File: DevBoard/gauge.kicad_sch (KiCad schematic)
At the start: 44 parts, among them J101 Pack (welded 4S) - use instea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, J102 Cell NTC 10k 103AT, J103 EV2400 SMBus, Q101 AGM404AP1, Q102 AGM404AP1, U101 BQ40Z50RSMR-R2

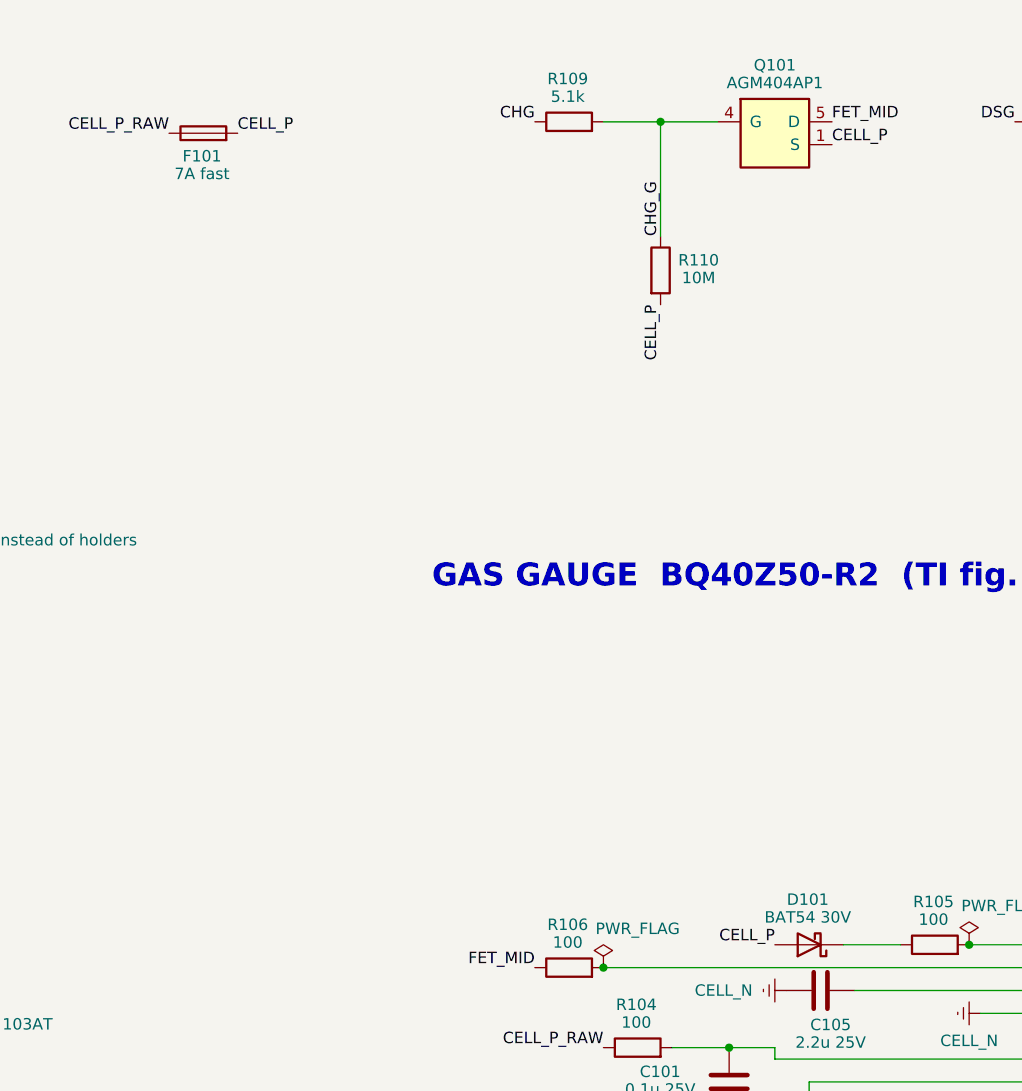
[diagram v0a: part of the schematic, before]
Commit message: Dev board: choose fuse, gauge diode and TPS25751 capacitor values
- F101: 1206FA-8A (C21261118), 1206, 32 V, 300 A interrupt; D101: BAT54WS (C7502694)
- TPS25751 caps per datasheet table 6.4 (after derating): LDO_3V3 and LDO_1V5
  to 10 uF, VBUS to 4.7 uF 50 V 0805, PP5V bulk to a 220 uF polymer
- README: PPHV bulk vs cSnkBulkPd and INA190 stock as open items

Co-Authored-By: Claude Opus 5.5 <noreply@anthropic.com>
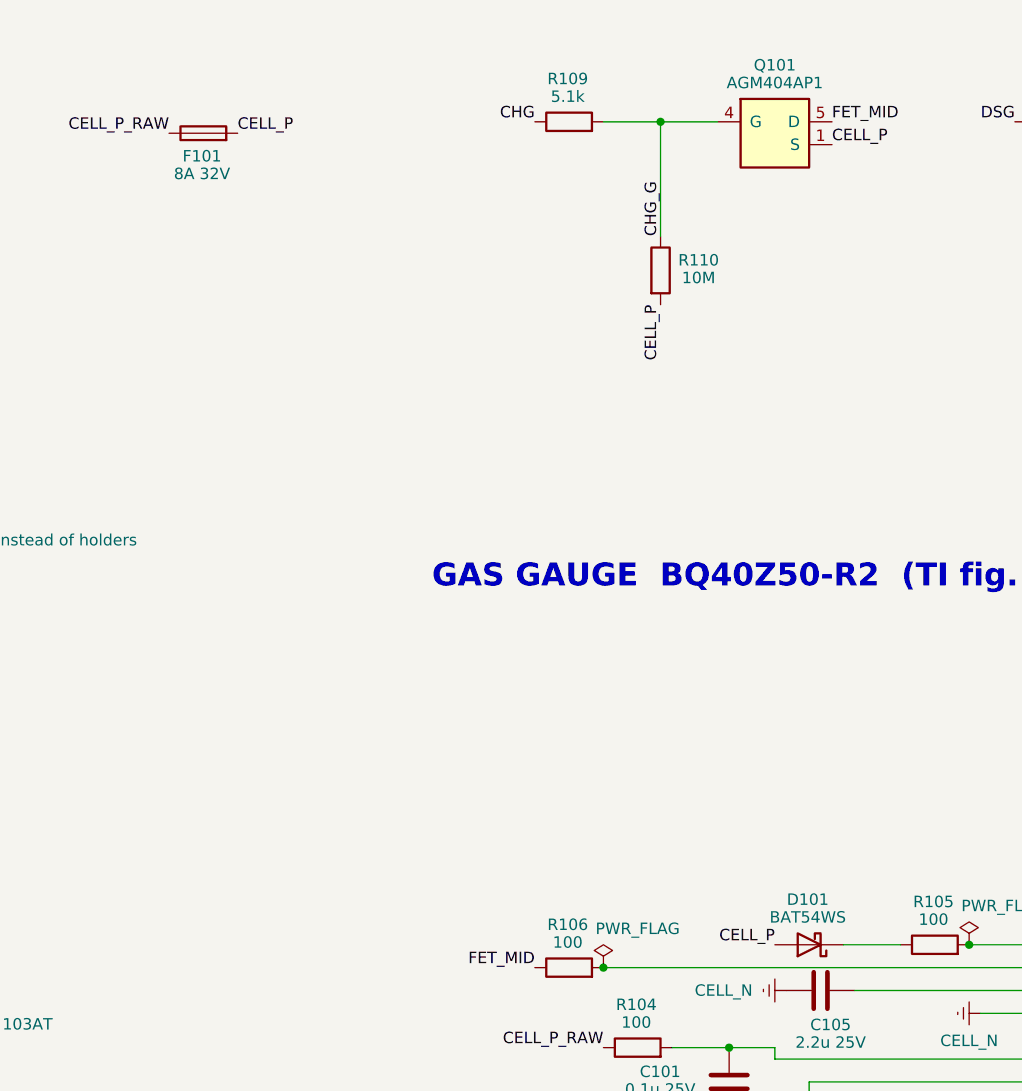
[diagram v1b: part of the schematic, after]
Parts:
- D101: value BAT54 30V -> BAT54WS; LCSC (none) -> C7502694
- F101: value 7A fast -> 8A 32V; footprint Fuse:Fuse_2512_6332Metric -> Fuse:Fuse_1206_3216Metric; LCSC (none) -> C21261118; MPN (none) -> prosemi 1206FA-8A; Notes part TBD -> fast; 300 A @ 24 V interrupt; ~6 A continuous after 75 % de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
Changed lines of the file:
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@@
 	)
 	(junction
+		(at 196.85 135.89)
+		(diameter 0)
+		(color 0 0 0 0)
+	)
+	(junction
 		(at 198.12 181.61)
 		(diameter 0)
@@
 	)
 	(junction
+		(at 215.9 44.45)
+		(diameter 0)
+		(color 0 0 0 0)
+	)
+	(junction
+		(at 162.56 44.45)
+		(diameter 0)
+		(color 0 0 0 0)
+	)
+	(junction
+		(at 156.21 138.43)
+		(diameter 0)
+		(color 0 0 0 0)
+	)
+	(junction
 		(at 233.68 158.75)
 		(diameter 0)
@@
 			)
 		)
-		(property "Value" "BAT54 30V"
+		(property "Value" "BAT54WS"
 			(at 178.92 132.84 0)
 			(show_name no)
@@
 			)
 		)
+		(property "LCSC" "C7502694"
+			(at 179.07 135.89 0)
+			(hide yes)
+			(show_name no)
+			(do_not_autoplace no)
+			(effects
+				(font
+					(size 1.27 1.27)
+				)
+			)
+		)
 		(pin "1"
 		)
@@
 			)
 		)
-		(property "Value" "7A fast"
+		(property "Value" "8A 32V"
 			(at 111.61 50.23 90)
 			(show_name no)
@@
 			)
 		)
-		(property "Footprint" "Fuse:Fuse_2512_6332Metric"
+		(property "Footprint" "Fuse:Fuse_1206_3216Metric"
 			(at 111.76 47.498 90)
 			(hide yes)
@@
 			)
 		)
-		(property "Notes" "part TBD"
+		(property "Notes" "fast; 300 A @ 24 V interrupt; ~6 A continuous after 75 % derating"
 			(at 0 0 0)
 			(hide yes)
@@
 			)
 		)
+		(property "LCSC" "C21261118"
+			(at 111.76 45.72 0)
+			(hide yes)
+			(show_name no)
+			(do_not_autoplace no)
+			(effects
+				(font
+					(size 1.27 1.27)
+				)
+			)
+		)
+		(property "MPN" "prosemi 1206FA-8A"
+			(at 111.76 45.72 0)
+			(hide yes)
+			(show_name no)
+			(do_not_autoplace no)
+			(effects
+				(font
+					(size 1.27 1.27)
+				)
+			)
+		)
 		(pin "1"
 		)
@@
 		)
 	)
-	(junction
-		(at 156.21 138.43)
-		(diameter 0)
-		(color 0 0 0 0)
-	)
-	(junction
-		(at 196.85 135.89)
-		(diameter 0)
-		(color 0 0 0 0)
-	)
-	(junction
-		(at 162.56 44.45)
-		(diameter 0)
-		(color 0 0 0 0)
-	)
-	(junction
-		(at 215.9 44.45)
-		(diameter 0)
-		(color 0 0 0 0)
-	)
 	(sheet_instances

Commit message: Dev board: project footprints for holder, USB-C, half-bridge, module, EEPROM, BQ25756
- tools/make_footprints.py generates MonolithDev.pretty from the datasheets:
  BH-21700-B1BJ001 holder, Shou Han USB-C (with board-edge cutout),
  Infineon PG-TDSON-8-57 half-bridge (land + stencil), STM32WB1MMC LGA77,
  ST UFDFPN8 2x3 with the correct 1.2x1.4 exposed pad, and a 10 A net tie
- BQ25756 RRV0036A footprint from Antmicro (Apache-2.0), checked against TI
- Footprints assigned; R430/R530 become net-tie links, off the BOM and CPL
- Every symbol pin has a pad and vice versa; nets, ERC and overlaps unchanged

Co-Authored-By: Claude Opus 5.5 <noreply@anthropic.com>
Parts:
- BT101, BT102, BT103, BT104: footprint (none) -> MonolithDev:BatteryHolder_MYOUNG_BH-21700-B1BJ001
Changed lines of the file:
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@@
 		(dnp no)
 		(property "Reference" "U101"
-			(at 215.90 129.60 0)
+			(at 215.9 129.6 0)
 			(show_name no)
 			(do_not_autoplace no)
@@
 		)
 		(property "Value" "BQ40Z50RSMR-R2"
-			(at 215.90 131.57 0)
+			(at 215.9 131.57 0)
 			(show_name no)
 			(do_not_autoplace no)
@@
 		(dnp no)
 		(property "Reference" "C107"
-			(at 243.80 82.69 0)
+			(at 243.8 82.69 0)
 			(show_name no)
 			(do_not_autoplace no)
@@
 		)
 		(property "Value" "0.1u 50V"
-			(at 243.80 84.65 0)
+			(at 243.8 84.65 0)
 			(show_name no)
 			(do_not_autoplace no)
@@
 		(dnp no)
 		(property "Reference" "TP106"
-			(at 266.70 44.95 0)
+			(at 266.7 44.95 0)
 			(show_name no)
 			(do_not_autoplace no)
@@
 		)
 		(property "Value" "GND"
-			(at 91.44 238.00 0)
+			(at 91.44 238 0)
 			(show_name no)
 			(do_not_autoplace no)
@@
 		)
 		(property "Value" "PACK_P"
-			(at 266.70 55.12 0)
+			(at 266.7 55.12 0)
 			(show_name no)
 			(do_not_autoplace no)
@@
 		)
 		(property "Value" "PACK_P"
-			(at 215.90 69.09 0)
+			(at 215.9 69.09 0)
 			(show_name no)
 			(do_not_autoplace no)
@@
 		(dnp no)
 		(property "Reference" "C108"
-			(at 243.80 97.93 0)
+			(at 243.8 97.93 0)
 			(show_name no)
 			(do_not_autoplace no)
@@
 		)
 		(property "Value" "0.1u 50V"
-			(at 243.80 99.89 0)
+			(at 243.8 99.89 0)
 			(show_name no)
 			(do_not_autoplace no)
@@
 		(dnp no)
 		(property "Reference" "TP104"
-			(at 76.20 258.31 0)
+			(at 76.2 258.31 0)
 			(show_name no)
 			(do_not_autoplace no)
@@
 		(dnp no)
 		(property "Reference" "BT101"
-			(at 38.10 146.41 0)
+			(at 38.1 146.41 0)
 			(show_name no)
 			(do_not_autoplace no)
@@
 		)
 		(property "Value" "BH-21700-B1BJ001"
-			(at 38.10 148.38 0)
+			(at 38.1 148.38 0)
 			(show_name no)
 			(do_not_autoplace no)
@@
 			)
 		)
-		(property "Footprint" ""
+		(property "Footprint" "MonolithDev:BatteryHolder_MYOUNG_BH-21700-B1BJ001"
 			(at 38.1 141.224 90)
 			(hide yes)
@@
 		(dnp no)
 		(property "Reference" "BT102"
-			(at 50.84 111.90 0)
+			(at 50.84 111.9 0)
 			(show_name no)
 			(do_not_autoplace no)
@@
 			)
 		)
-		(property "Footprint" ""
+		(property "Footprint" "MonolithDev:BatteryHolder_MYOUNG_BH-21700-B1BJ001"
 			(at 38.1 115.824 90)
 			(hide yes)
@@
 		(dnp no)
 		(property "Reference" "Q102"
-			(at 228.60 38.16 0)
+			(at 228.6 38.16 0)
 			(show_name no)
 			(do_not_autoplace no)
@@
 		)
 		(property "Value" "AGM404AP1"
-			(at 228.60 40.13 0)
+			(at 228.6 40.13 0)
 			(show_name no)
 			(do_not_autoplace no)
@@
 		(dnp no)
 		(property "Reference" "R103"
-			(at 152.85 156.50 90)
+			(at 152.85 156.5 90)
 			(show_name no)
 			(do_not_autoplace no)
@@
 		(dnp no)
 		(property "Reference" "BT104"
-			(at 50.84 61.10 0)
+			(at 50.84 61.1 0)
 			(show_name no)
 			(do_not_autoplace no)
@@
 			)
 		)
-		(property "Footprint" ""
+		(property "Footprint" "MonolithDev:BatteryHolder_MYOUNG_BH-21700-B1BJ001"
 			(at 38.1 65.024 90)
 			(hide yes)
@@
 		)
 		(property "Value" "CELL_N"
-			(at 228.60 193.55 0)
+			(at 228.6 193.55 0)
 			(show_name no)
 			(do_not_autoplace no)
@@
 		(dnp no)
 		(property "Reference" "BT103"
-			(at 50.84 86.50 0)
+			(at 50.84 86.5 0)
 			(show_name no)
 			(do_not_autoplace no)
@@
 			)
 		)
-		(property "Footprint" ""
+		(property "Footprint" "MonolithDev:BatteryHolder_MYOUNG_BH-21700-B1BJ001"
 			(at 38.1 90.424 90)
 			(hide yes)
@@
 		)
 		(property "Value" "PWR_FLAG"
-			(at 190.50 259.84 0)
+			(at 190.5 259.84 0)
 			(show_name no)
 			(do_not_autoplace no)
@@
 		)
 		(property "Value" "0.1u 25V"
-			(at 177.84 167.20 0)
+			(at 177.84 167.2 0)
 			(show_name no)
 			(do_not_autoplace no)
@@
 		(dnp no)
 		(property "Reference" "C101"
-			(at 162.52 150.00 0)
+			(at 162.52 150 0)
 			(show_name no)
 			(do_not_autoplace no)
@@
 		)
 		(property "Value" "100"
-			(at 98.91 225.80 90)
+			(at 98.91 225.8 90)
 			(show_name no)
 			(do_not_autoplace no)

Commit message: Dev board: board setup (175x115, 4L 0.8 mm), netlist loaded, PDFN fix
- Board: 175 x 115 mm (the four holders need ~96 x 110), 4 layers 0.8 mm,
  2 oz outer / 1 oz inner, ENIG stack-up; six M3 board-only holes; outline
  broken for the two USB-C notches, J401/J501 placed and locked on the right edge
- JLC rules, via/track presets, net classes (HighCurrent, Power, GND,
  GateDrive) and custom rules in MonolithDev.kicad_dru (tools/setup_board.py)
- Netlist loaded with tools/netlist_to_board.py (the MCP sync merged the two
  ports' nets); kicad-cli parity check reports 0 issues
- Q101/Q102: AGM404AP1 is a 3.3x3.3 PDFN, not TDSON-8 (5x6); new footprint
- USB-C signal pads moved 0.2 mm in from the notch for JLC's edge clearance
- Production notes: notch is 5.65 mm deep (not 4.7), flange sticks out ~1.95 mm

Co-Authored-By: Claude Opus 5.5 <noreply@anthropic.com>
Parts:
- Q101, Q102: footprint Package_TO_SOT_SMD:TDSON-8-1 -> MonolithDev:AGM_PDFN-8_3.3x3.3mm_P0.65mm
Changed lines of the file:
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@@
 			)
 		)
-		(property "Footprint" "Package_TO_SOT_SMD:TDSON-8-1"
+		(property "Footprint" "MonolithDev:AGM_PDFN-8_3.3x3.3mm_P0.65mm"
 			(at 175.26 45.72 0)
 			(hide yes)
@@
 			)
 		)
-		(property "Footprint" "Package_TO_SOT_SMD:TDSON-8-1"
+		(property "Footprint" "MonolithDev:AGM_PDFN-8_3.3x3.3mm_P0.65mm"
 			(at 228.6 45.72 0)
 			(hide yes)

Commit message: Dev board rev A4: design-review fixes, polymer bulk, charge inhibit
Schematic design review (three reviewers, cross-challenged) in
docs/devboard/schematic-review-2026-10-12.md, and its fixes:
- U203 TPS70950 EN no longer tied to PACK_P (would destroy it)
- ICHG 17.8k: 2.8 A per port (was 9.8 A, above the cells' 5.6 A)
- U101 footprint from TI RSM0032A (1.4 mm thermal pad, was 2.8 mm)
- D+/D- ESD now 5 V PESD5V0S2BT (TPS25751 GPIO4/5 are rated 6 V)
- R101-R104 1206, F101 and J101 DNP, DNP gate parts on Q102
- BTP_INT buffered by a 2N7002; SMBus pull-ups on a removable 0R
- Wake button, bench PACK_P header, reset, BOOT0/3V3_SLEEP pads,
  J303 series resistors, IRQ pull-ups, vertical SMAs, BOM ratings

Open-question decisions: CHG_INH (PB8 -> each BQ25756 CE) lets the
MCU stop charging independently of the TPS25751; J103 in EV2400
SMBus pin order; "fit cells before USB" silkscreen.

Charger bulk banks now one solid polymer cap plus the MLCCs at the
FETs (16 fewer MLCCs). PWR_FLAGs moved to where each rail is sourced.
Board: footprints swapped/added and placed, DRC clean before routing.

Co-Authored-By: Claude Opus 5.5 <noreply@anthropic.com>
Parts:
- added C109: 0.1u 50V, Capacitor_SMD:C_0603_1608Metric, symbol Device:C
- added D102: 1N4148WS, Diode_SMD:D_SOD-323, symbol Device:D
- added D103: BZT52C15, Diode_SMD:D_SOD-123, symbol Device:D_Zener
- added J104: Bench PACK_P, Connector_PinHeader_2.54mm:PinHeader_1x02_P2.54mm_Vertical, symbol Connector_Generic:Conn_01x02
- added Q103: 2N7002, Package_TO_SOT_SMD:SOT-23, symbol Transistor_FET:Q_NMOS_GSD
- added R117: 470k, Resistor_SMD:R_0603_1608Metric, symbol Device:R
- added R118: 4.7k, Resistor_SMD:R_0603_1608Metric, symbol Device:R
- added SW101: WAKE, Button_Switch_SMD:SW_Push_1P1T_XKB_TS-1187A, symbol Switch:SW_Push
- C105: value 2.2u 25V -> 2.2u 50V; footprint Capacitor_SMD:C_0603_1608Metric -> Capacitor_SMD:C_0805_2012Metric; LCSC (none) -> C2762602; MPN (none) -> CL21B225KBYNNNE; Notes (none) -> PBI sits near VBAT (16.8 V): 50 V X7R 0805 keeps most of it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
- C106: value 0.1u -> 0.1u 50V; LCSC (none) -> C14663; MPN (none) -> CC0603KRX7R9BB104
- F101: Notes fast; 300 A @ 24 V interrupt; ~6 A continuous after 75 % de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 -> Hand-fit after checking all four cells at TP102-TP105 (JLC 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; now not fitted
- J101: Notes (none) -> Fit only when the welded pack is used, and never with cells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; now not fitted
- J103: footprint Connector_PinHeader_2.54mm:PinHeader_1x03_P2.54mm_Vertical -> Connector_PinHeader_2.54mm:PinHeader_1x04_P2.54mm_Vertical; symbol Connector_Generic:Conn_01x03 -> Connector_Generic:Conn_01x04; Notes (none) -> Same pin order as the EV2400 SMBus port (SLUU446D): 1 VSS, 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
- R101, R102, R103, R104: footprint Resistor_SMD:R_0603_1608Metric -> Resistor_SMD:R_1206_3216Metric; LCSC (none) -> C17901; MPN (none) -> 1206W4F1000T5E; Notes (none) -> 1206 (0.25 W): survives the open-cell fault current until C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
- U101: footprint Package_DFN_QFN:VQFN-32-1EP_4x4mm_P0.4mm_EP2.8x2.8mm -> MonolithDev:TI_RSM0032A_VQFN-32_4x4mm_P0.4mm_EP1.4x1.4mm
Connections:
- net CELL_N: now also R117.2
- net CELL_P: now also SW101.1
- net DSG: now also D102.1 (K)
- net DSG_G: now also C109.1, D102.2 (A), D103.1 (K)
- net GAUGE_BTP: now also Q103.3 (D); no longer U101.15 (BTP_INT)
- net GND: now also J103.1 (Pin_1), C109.2, J104.2 (Pin_2), Q103.2 (S); no longer J103.3 (Pin_3)
- net PACK_P: now also D103.2 (A), J104.1 (Pin_1), R118.2
- net SCL: now also J103.2 (Pin_2); no longer J103.1 (Pin_1)
- net SDA: now also J103.3 (Pin_3); no longer J103.2 (Pin_2)
- new net: R118.1, SW101.2
- new net BTP_INT: Q103.1 (G), R117.1, U101.15 (BTP_INT)
- no-connect marks 5 -> 6
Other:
- note added: "Holders BT101-BT104 OR welded pack on J101 - never both. F101 and J101 are DNP: check each cell at TP102-TP105, then hand-fit F101."
- note added: "WAKE + BENCH SUPPLY"
- note removed: "Holders BT101-BT104 OR welded pack on J101 - never both. Check each cell at TP103-TP105 before fitting F101."

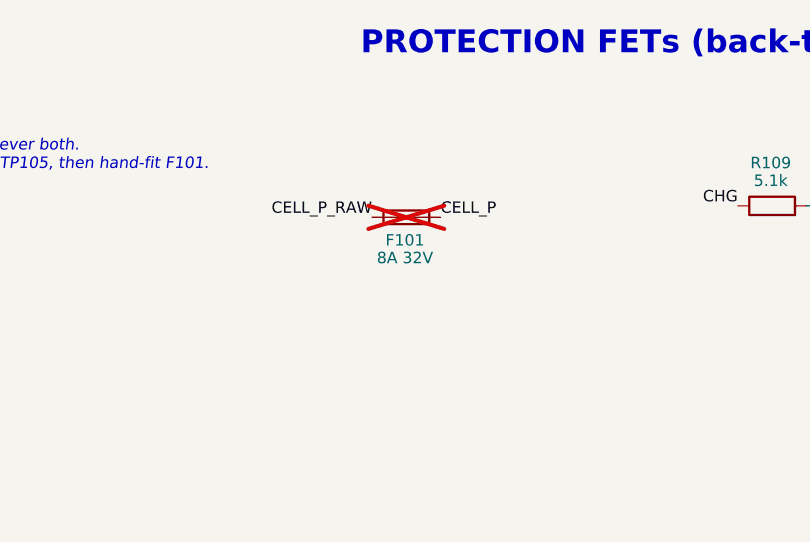
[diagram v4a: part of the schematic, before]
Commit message: Dev board: F101 15 A (1206FA-15A) for 100 W output
The 8 A fuse allowed about 6 A continuous after derating, 60-70 W out,
short of the 100 W goal (~10 A from the pack at the 12 V low end).
prosemi 1206FA-15A (C2838894): same 1206 footprint and 300 A at 24 Vdc
interrupt rating. Review doc: gauge OLD ~16-20 A, OCD1 ~10-11 A (2-3 A
in holder mode), output power sharing at 100 W total.

Co-Authored-By: Claude Opus 5.5 <noreply@anthropic.com>
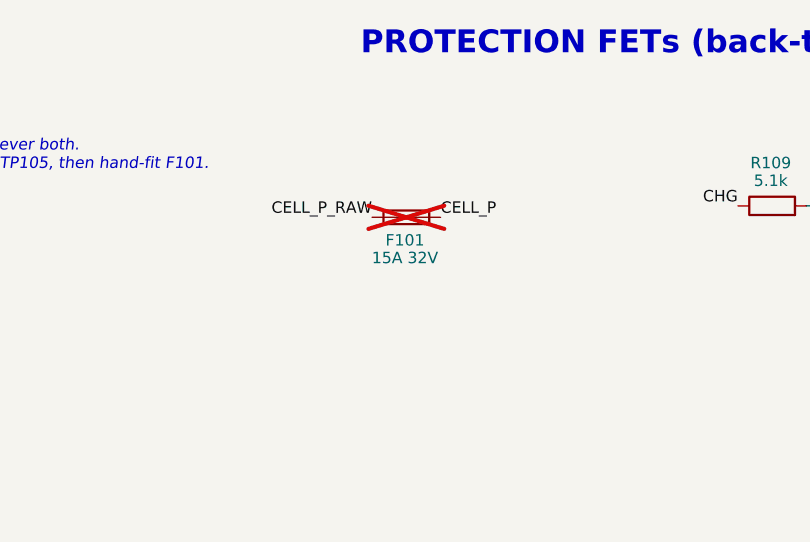
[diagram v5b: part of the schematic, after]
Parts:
- F101: value 8A 32V -> 15A 32V; LCSC C21261118 -> C2838894; MPN prosemi 1206FA-8A -> prosemi 1206FA-15A; Notes Hand-fit after checking all four cells at TP102-TP105 (JLC leaves it off). prosemi 1206FA-8A, LCSC C21261118 -> Hand-fit after checking all four cells at TP102-TP105 (JLC leaves it off). 15 A for 100 W out at the 12 V low end (~10 A continuous, 75 % derating). Interrupt 300 A at 24 Vdc (pack max 16.8 V). 3.9 mOhm: 0.4 W at 10 A, give it copper
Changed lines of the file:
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@@
 			)
 		)
-		(property "Value" "8A 32V"
+		(property "Value" "15A 32V"
 			(at 111.61 50.23 90)
 			(show_name no)
@@
 			)
 		)
-		(property "Notes" "Hand-fit after checking all four cells at TP102-TP105 (JLC leaves it off). prosemi 1206FA-8A, LCSC C21261118"
+		(property "Notes" "Hand-fit after checking all four cells at TP102-TP105 (JLC leaves it off). 15 A for 100 W out at the 12 V low end (~10 A continuous, 75 % derating). Interrupt 300 A at 24 Vdc (pack max 16.8 V). 3.9 mOhm: 0.4 W at 10 A, give it copper"
 			(at 0 0 0)
 			(hide yes)
@@
 			)
 		)
-		(property "LCSC" "C21261118"
+		(property "LCSC" "C2838894"
 			(at 111.76 45.72 0)
 			(hide yes)
@@
 			)
 		)
-		(property "MPN" "prosemi 1206FA-8A"
+		(property "MPN" "prosemi 1206FA-15A"
 			(at 111.76 45.72 0)
 			(hide yes)
